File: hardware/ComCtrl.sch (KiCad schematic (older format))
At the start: 8 parts, among them K1 G5V-2-DC12, K2 G5V-2-DC12, U6 H11AA1

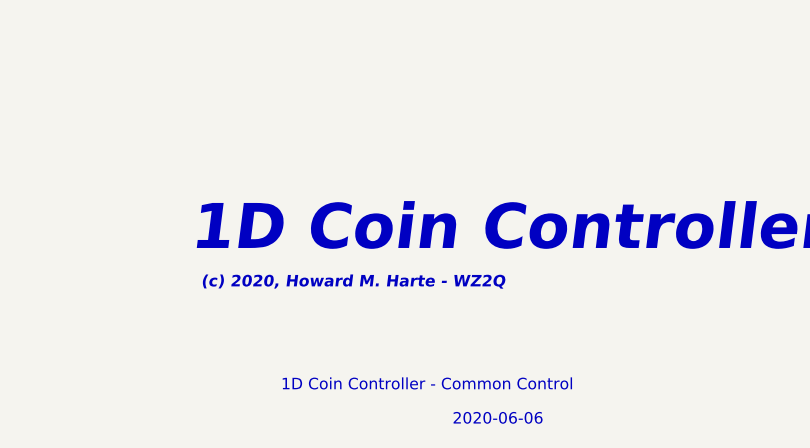
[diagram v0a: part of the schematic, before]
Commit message: Issue 2 schmatic and Layout
Added polarity reversal detection to monitor answer supervision.
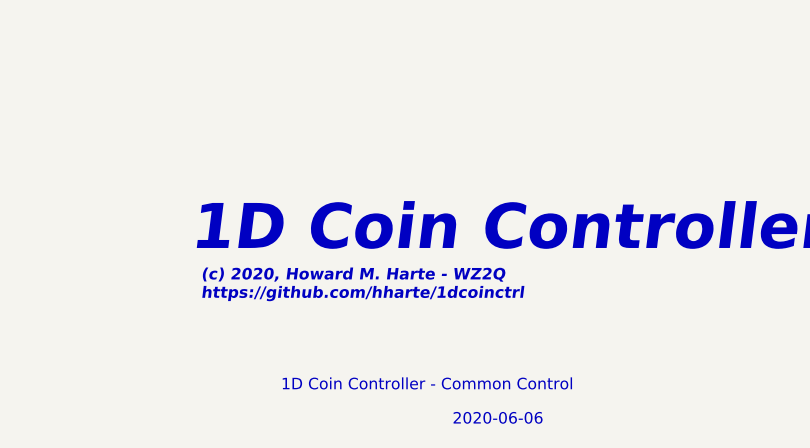
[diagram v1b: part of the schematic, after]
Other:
- note added: "(c) 2020, Howard M. Harte - WZ2Q\nhttps://github.com/hharte/1dcoinctrl"
- note removed: "(c) 2020, Howard M. Harte - WZ2Q"
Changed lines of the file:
@@
 Text Notes 7050 6900 0    197  Italic 39
 1D Coin Controller
-Text Notes 7100 7050 0    50   Italic 10
-(c) 2020, Howard M. Harte - WZ2Q
 Text Notes 10600 7650 0    50   ~ 0
 1
@@
 Text Notes 8200 7650 0    50   ~ 0
 2020-06-06
+Text Notes 7100 7100 0    50   Italic 10
+(c) 2020, Howard M. Harte - WZ2Q\nhttps://github.com/hharte/1dcoinctrl
 $EndSCHEMATC
